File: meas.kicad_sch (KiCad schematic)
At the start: 13 parts, among them J101 Conn_01x06_Socket, J102 Conn_01x02_Socket, J103 Conn_01x02_Socket, J104 Conn_01x02_Socket, J105 Conn_01x02_Socket

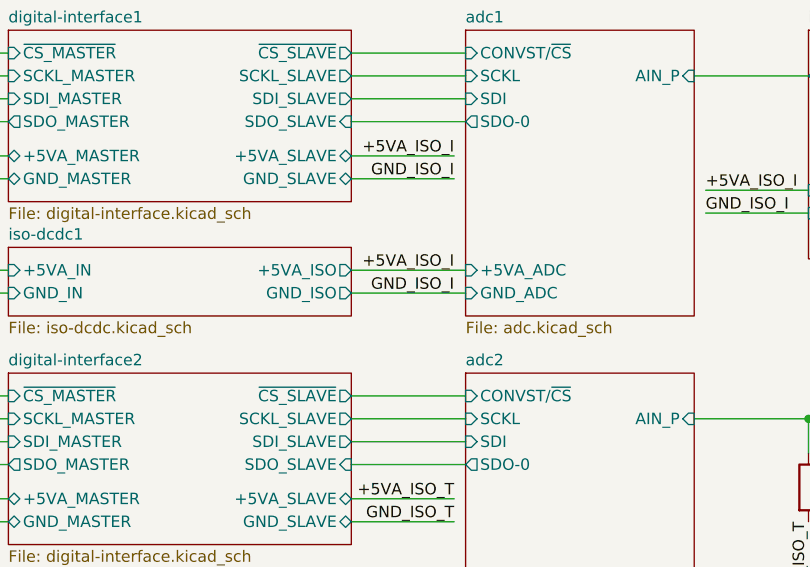
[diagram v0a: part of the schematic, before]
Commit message: fix netlist error in schematic and layout
GND planes of isodcdc and adc of current measurement were not connected and now are connected.
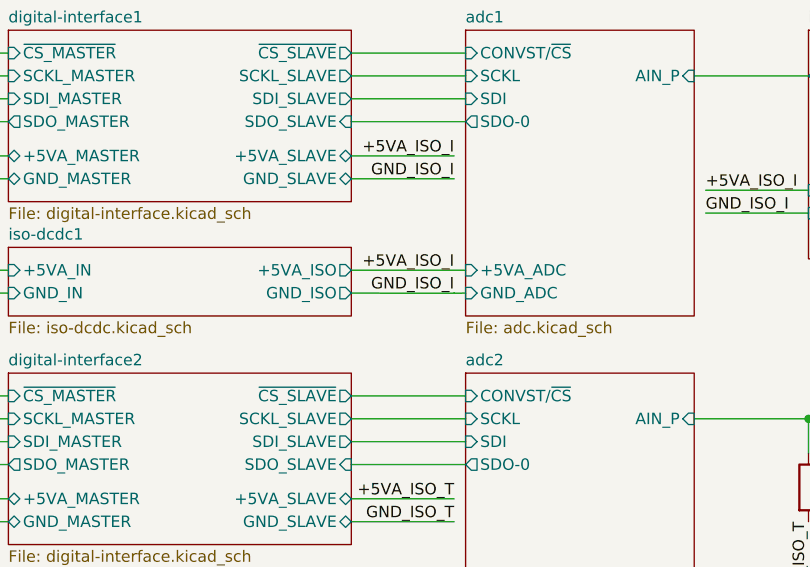
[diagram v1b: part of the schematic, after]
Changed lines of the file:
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@@
 	(title_block
 		(title "Measurement")
-		(date "2025-02-23")
-		(rev "1.0.0")
+		(date "2025-03-06")
+		(rev "2.0.0")
 		(company "Open Battery Tester")
 		(comment 1 "Overview")
@@
 	(wire
 		(pts
+			(xy 176.53 105.4269) (xy 176.526 105.4269)
+		)
+		(stroke
+			(width 0)
+			(type default)
+		)
+	)
+	(wire
+		(pts
 			(xy 165.1 83.82) (xy 177.8 83.82)
 		)
@@
 	(wire
 		(pts
+			(xy 176.526 105.4269) (xy 177.8 105.41)
+		)
+		(stroke
+			(width 0)
+			(type default)
+		)
+	)
+	(wire
+		(pts
 			(xy 48.26 64.77) (xy 48.26 52.07)
 		)
@@
 	(wire
 		(pts
-			(xy 165.1 105.41) (xy 177.8 105.41)
+			(xy 165.1 105.41) (xy 176.526 105.4269)
 		)
 		(stroke
@@
 		(pts
 			(xy 107.95 124.46) (xy 127 124.46)
+		)
+		(stroke
+			(width 0)
+			(type default)
+		)
+	)
+	(wire
+		(pts
+			(xy 176.53 105.3931) (xy 176.53 105.4269)
 		)
 		(stroke
@@
 	)
 	(label "GND_ISO_I"
-		(at 176.526 105.4269 180)
-		(fields_autoplaced yes)
-		(effects
+		(at 176.53 105.3931 180)
+		(fields_autoplaced yes)
+		(effects

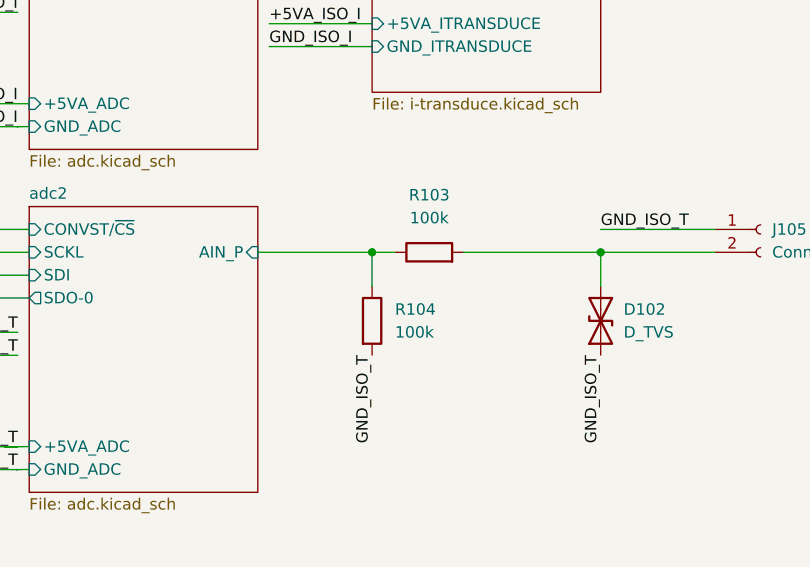
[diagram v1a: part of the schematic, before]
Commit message: change resitor divider for temperature input for higher accuracy
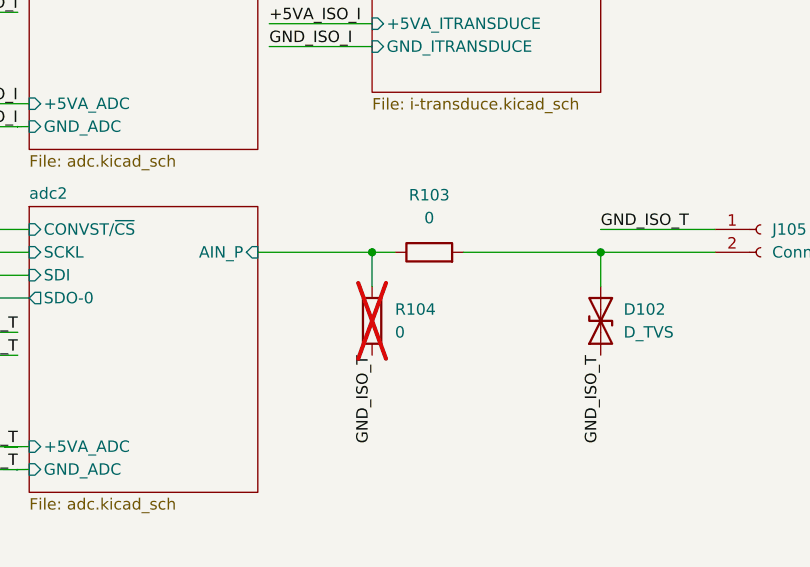
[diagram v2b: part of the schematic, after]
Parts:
- R103: value 100k -> 0; MPN RC1210FR-07100KL -> RC1210JR-070RL; VPN 603-RC1210FR-07100KL -> 603-RC1210JR-070RL
- R104: value 100k -> 0; MPN RC1210FR-07100KL -> RC1210JR-070RL; VPN 603-RC1210FR-07100KL -> 603-RC1210JR-070RL; now not fitted
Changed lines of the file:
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@@
 	(title_block
 		(title "Measurement")
-		(date "2025-03-06")
-		(rev "2.0.0")
+		(date "2025-03-08")
+		(rev "2.1.0")
 		(company "Open Battery Tester")
 		(comment 1 "Overview")
@@
 		(in_bom yes)
 		(on_board yes)
-		(dnp no)
+		(dnp yes)
 		(fields_autoplaced yes)
 		(property "Reference" "R104"
@@
 			)
 		)
-		(property "Value" "100k"
+		(property "Value" "0"
 			(at 218.44 128.2699 0)
 			(effects
@@
 			)
 		)
-		(property "MPN" "RC1210FR-07100KL"
+		(property "MPN" "RC1210JR-070RL"
 			(at 215.9 127 0)
 			(effects
@@
 			)
 		)
-		(property "VPN" "603-RC1210FR-07100KL"
+		(property "VPN" "603-RC1210JR-070RL"
 			(at 215.9 127 0)
 			(effects
@@
 			)
 		)
-		(property "Value" "100k"
+		(property "Value" "0"
 			(at 222.25 115.57 90)
 			(effects
@@
 			)
 		)
-		(property "MPN" "RC1210FR-07100KL"
+		(property "MPN" "RC1210JR-070RL"
 			(at 222.25 119.38 0)
 			(effects
@@
 			)
 		)
-		(property "VPN" "603-RC1210FR-07100KL"
+		(property "VPN" "603-RC1210JR-070RL"
 			(at 222.25 119.38 0)
 			(effects
